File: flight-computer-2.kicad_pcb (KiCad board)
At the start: 4 copper layers, 51 x 51 mm, 87 parts, among them J1 USB4105-GF-A, J2 THR, J3 SER1, J4 SER2, J5 SER3, J6 SER4, J7 Breakout L, J8 Breakout R, SW1 RESET, SW2 BOOT, U1 AP2114H-3.3TRG1, U2 MUN5214DW1T1G, U3 BNO080, U4 CP2102N, U5 MPL3115A2, U6 ESP32-PICO-D4, Y1 32.768kHz

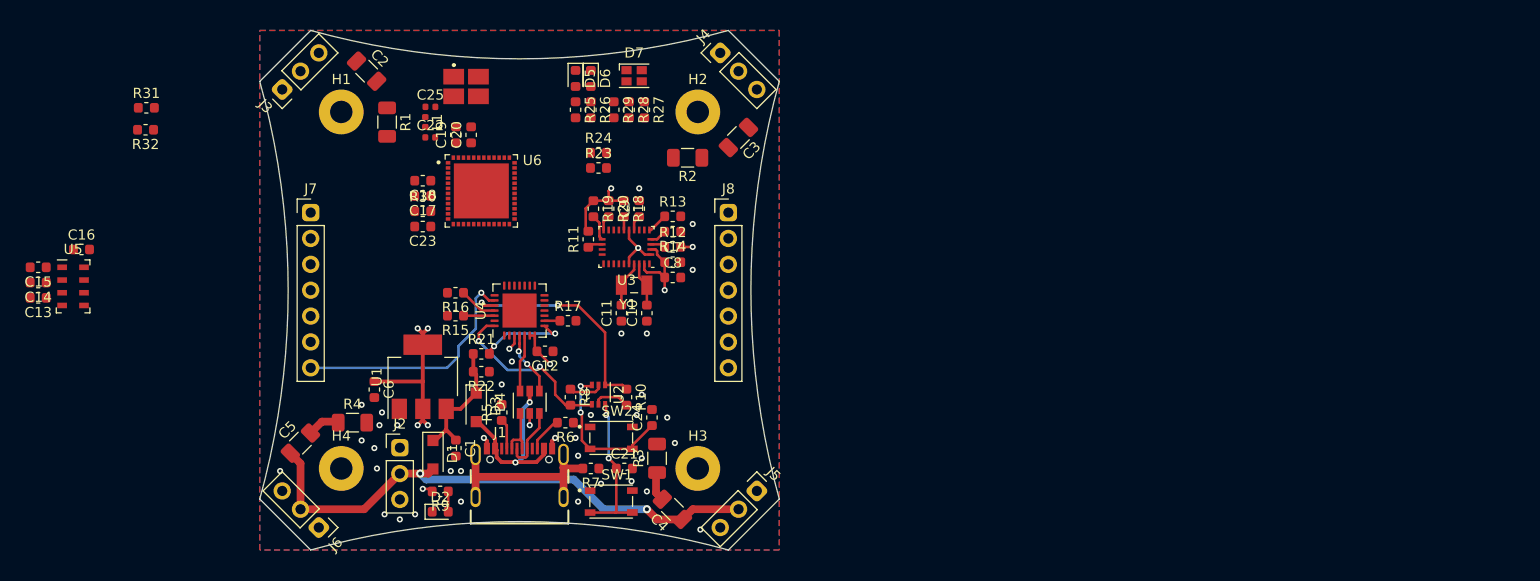
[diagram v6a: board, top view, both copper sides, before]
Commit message: USB/UART routing complete
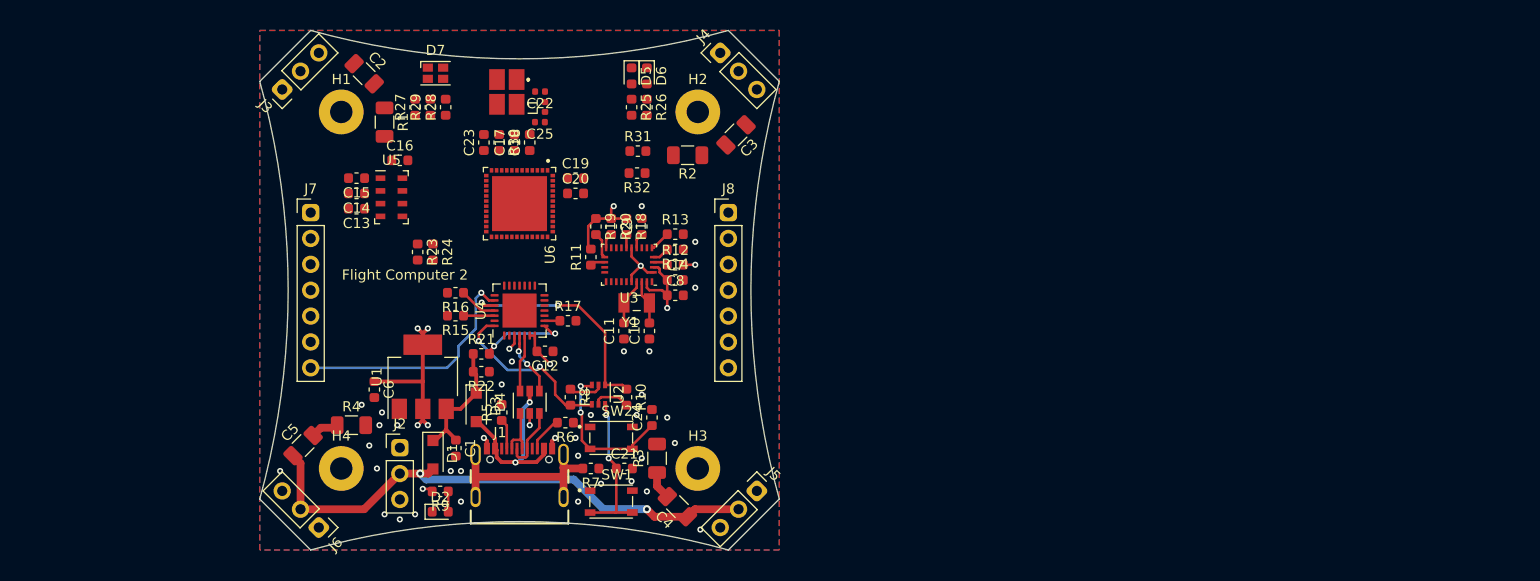
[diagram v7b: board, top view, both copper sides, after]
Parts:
- moved R31 48.4 mm to (109.1, 63.8)
- moved R32 48.4 mm to (109.0, 66.0)
- moved C13 32.5 mm to (81.5, 69.5)
- moved C14 32.5 mm to (81.5, 68.0)
- moved C15 32.5 mm to (81.5, 66.5)
- moved C16 32.5 mm to (85.8, 64.8)
- moved U5 32.5 mm to (84.9, 68.4)
- moved R27 22.5 mm to (87.2, 59.5), turned to 90 degrees
- moved R23 19.6 mm to (87.5, 73.8), turned to 270 degrees
- moved D7 19.5 mm to (89.2, 56.2)
- moved R24 19.0 mm to (89.0, 73.8), turned to 270 degrees
- moved R28 18.0 mm to (90.2, 59.5), turned to 90 degrees
- moved R29 18.0 mm to (88.8, 59.5), turned to 90 degrees
- moved C19 12.5 mm to (103.0, 66.5), turned to 0 degrees
- moved L1 11.8 mm to (100.0, 59.5), turned to 90 degrees
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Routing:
- net /VBEC: track 54.1 -> 53.5 mm
- net GND: vias 40 -> 39
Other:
- board text added: "Flight Computer 2"

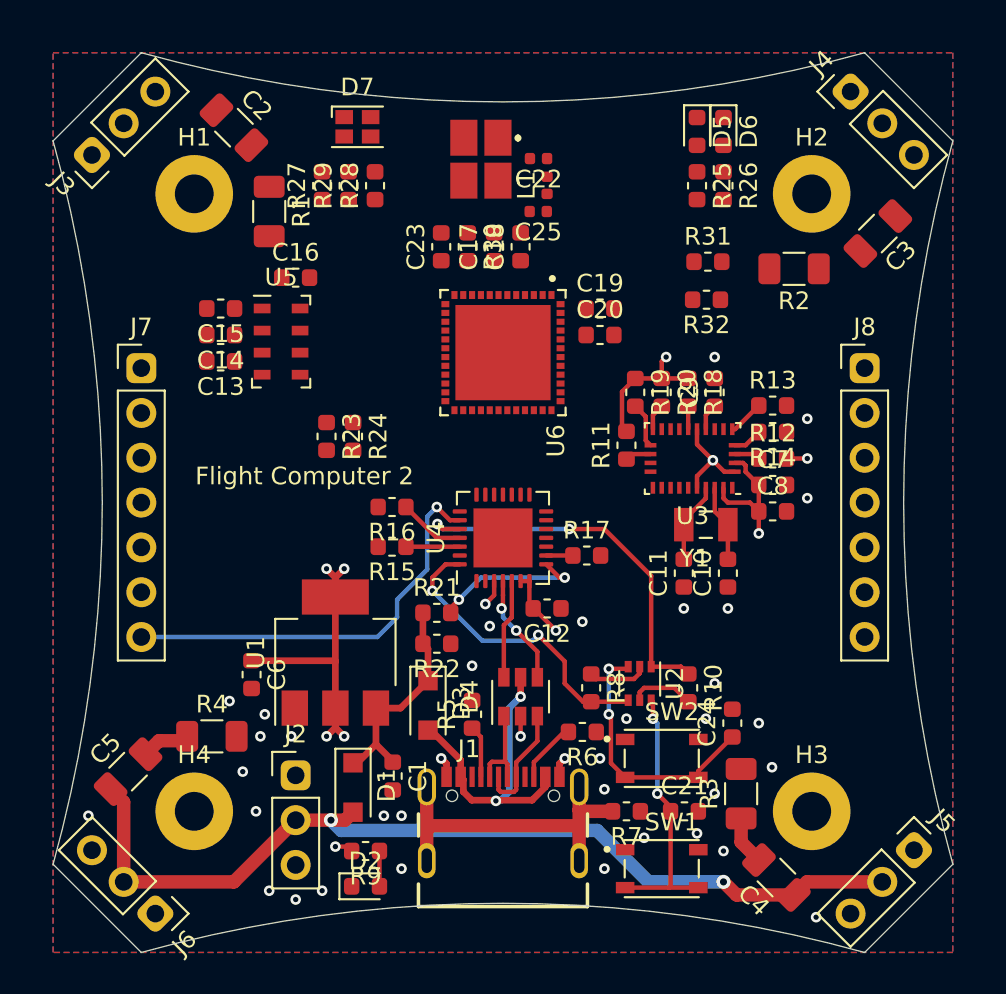
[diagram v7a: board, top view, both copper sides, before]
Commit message: MCU and sensor routing
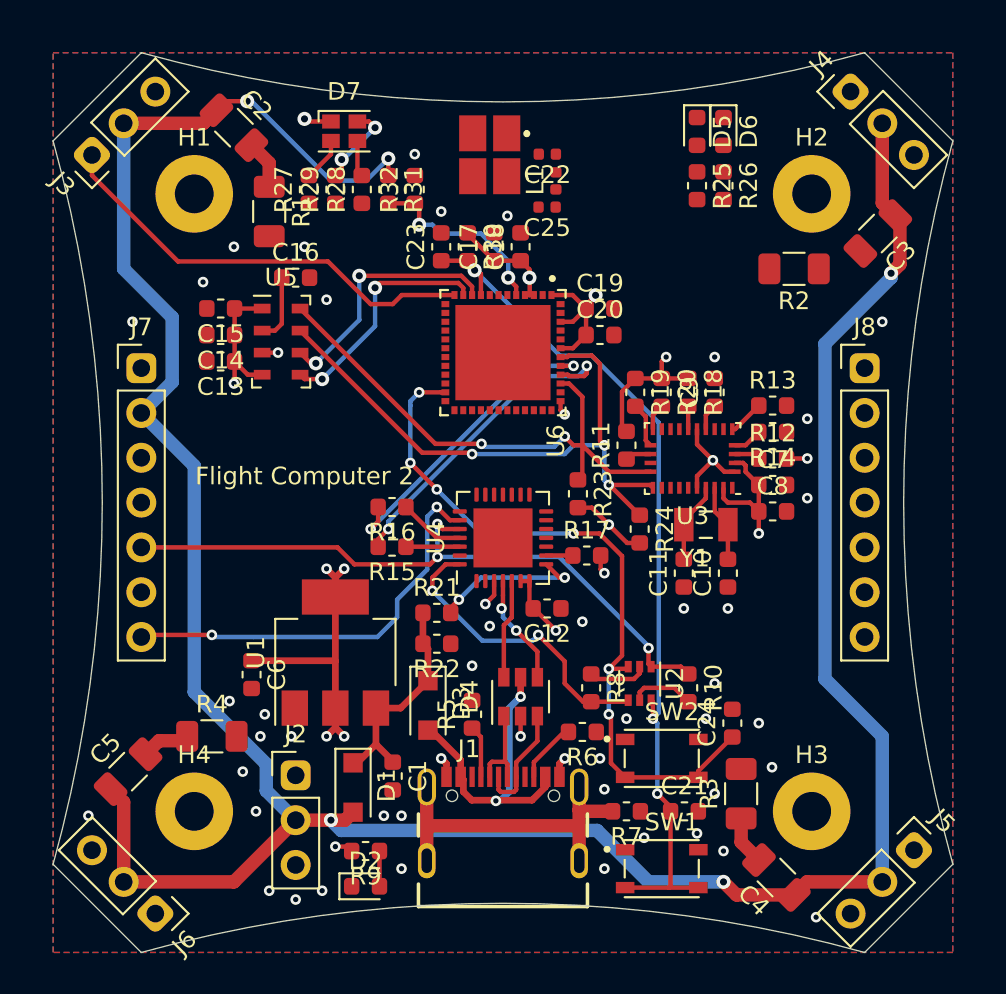
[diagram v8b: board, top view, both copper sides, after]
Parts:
- moved R31 18.6 mm to (91.0, 59.8), turned to 270 degrees
- moved R32 17.7 mm to (92.5, 59.8), turned to 90 degrees
- moved R24 17.1 mm to (105.2, 79.0)
- moved R23 14.6 mm to (101.8, 77.0)
- moved D7 0.79 mm to (88.5, 56.5)
- moved R27 0.78 mm to (86.5, 59.8)
- moved R28 0.78 mm to (89.5, 59.8)
- moved R29 0.78 mm to (88.0, 59.8)
- moved AE1 0.56 mm to (96.8, 57.8)
- moved C22 0.56 mm to (100.0, 57.8)
- moved C25 0.56 mm to (100.0, 60.8)
- moved L1 0.56 mm to (100.5, 59.3)
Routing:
- net /VBEC: track 53.5 -> 163.9 mm, vias 2 -> 5
- net /SDA: track 0.00 -> 34.9 mm, vias 0 -> 3
- net /EN: track 15.3 -> 50.0 mm, vias 2 -> 3
- net /SCL: track 0.00 -> 30.5 mm, vias 0 -> 2
- net +3V3: track 37.7 -> 68.2 mm, vias 9 -> 16
- net /IO0: track 14.9 -> 41.5 mm, vias 2 -> 6
- net /SER1: track 0.00 -> 24.9 mm
- net /RXD0: track 0.00 -> 18.8 mm, vias 0 -> 2
- net /TXD0: track 0.00 -> 17.5 mm, vias 0 -> 2
- net /RTS: track 22.1 -> 38.6 mm, vias 2 -> 3
- net /ALT_INT_1: track 0.00 -> 14.3 mm, vias 0 -> 2
- net /ALT_INT_2: track 0.00 -> 13.4 mm, vias 0 -> 2
- net /EXT_PWR: track 0.00 -> 10.8 mm, vias 0 -> 2
- net Net-(D7-Pad2): track 0.00 -> 4.88 mm, vias 0 -> 2
- net Net-(C16-Pad1): track 0.00 -> 3.89 mm
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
